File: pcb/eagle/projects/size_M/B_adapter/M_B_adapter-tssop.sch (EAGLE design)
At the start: 16 parts

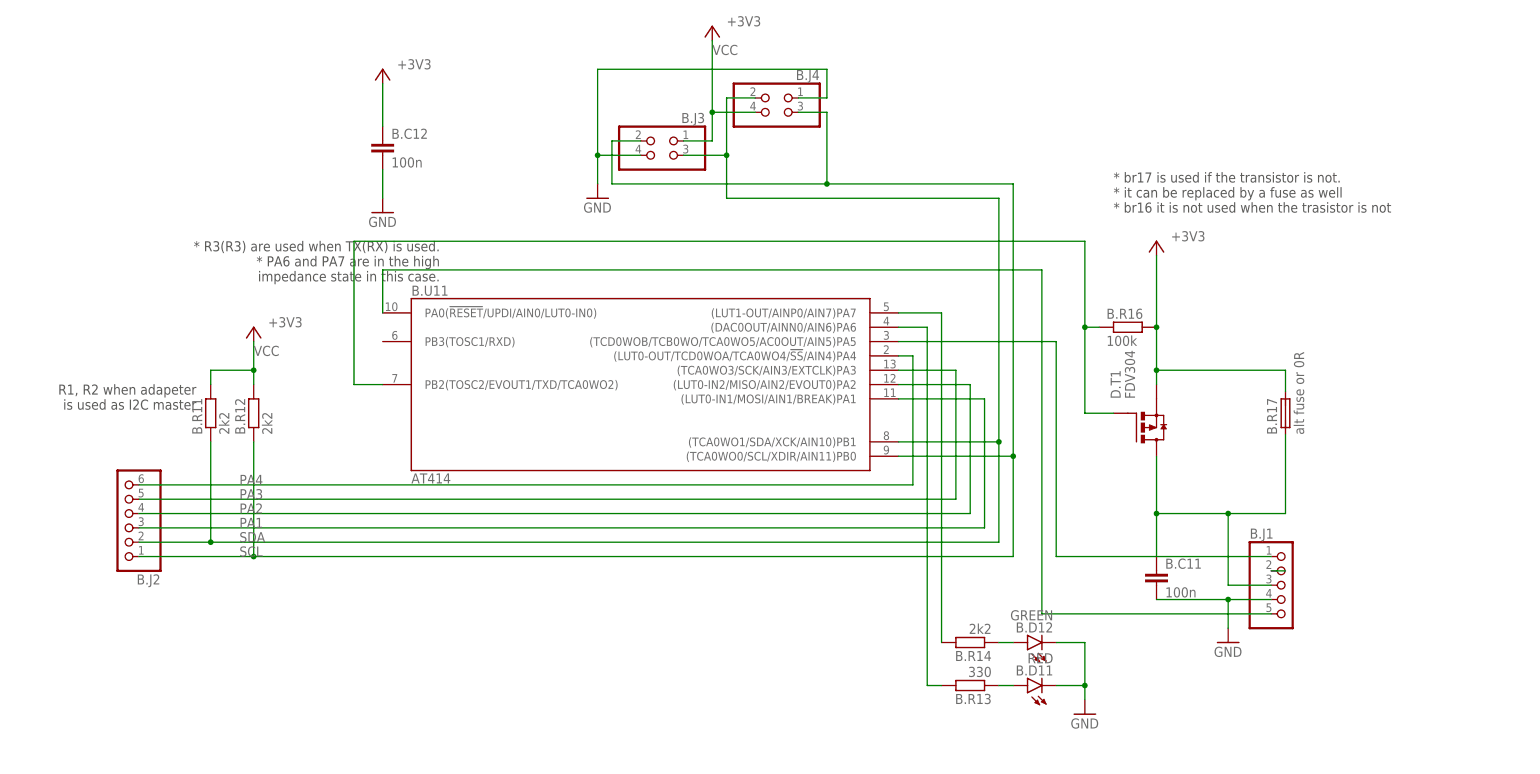
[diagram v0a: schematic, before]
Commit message: changed power sleep transistor to p-channel added tssop version for attiny v2 chips
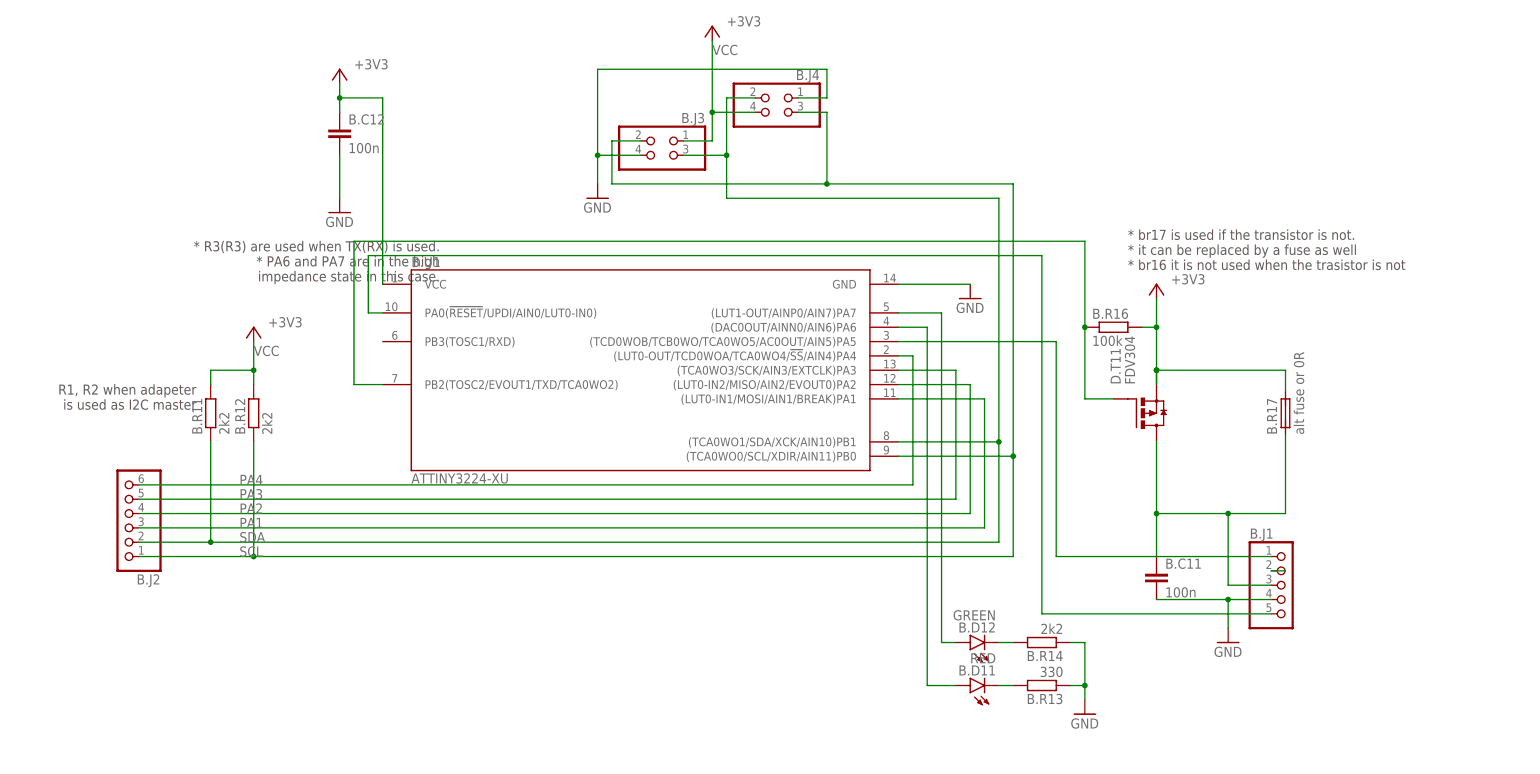
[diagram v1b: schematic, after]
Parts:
- removed B.U11: AT414, atmel:ATTINY414-SSN
- removed D.T1: FDV304, hugo:P-MOSFET
- added B.U1: ATTINY3224-XU, ATTINY412-SSN:ATTINY3224-XU
- added D.T11: FDV304, hugo:P-MOSFET
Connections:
- removed net N$4: B.C11.1, B.J1.3, B.R17.1, D.T1.D
- removed net PA51: B.D11.A, B.R13.1
- new net N$1: B.D12.C, B.R14.2
- new net N$2: B.D11.C, B.R13.2
- net GND: now also B.R13.1, B.R14.1, B.U1.GND; no longer B.D11.C, B.D12.C
- net N$3: now also B.C11.1, B.J1.3, B.R17.1, D.T11.D; no longer B.D12.A, B.R14.1
- net N$5: now also B.D11.A, B.U1.(DAC0OUT/AINN0/AIN6)PA6; no longer B.R13.2, B.U11G$1.(DAC0OUT/AINN0/AIN6)PA6
- net PA1: now also B.U1.(LUT0-IN1/MOSI/AIN1/BREAK)PA1; no longer B.U11G$1.(LUT0-IN1/MOSI/AIN1/BREAK)PA1
- net PA2: now also B.U1.(LUT0-IN2/MISO/AIN2/EVOUT0)PA2; no longer B.U11G$1.(LUT0-IN2/MISO/AIN2/EVOUT0)PA2
- net PA3: now also B.U1.(TCA0WO3/SCK/AIN3/EXTCLK)PA3; no longer B.U11G$1.(TCA0WO3/SCK/AIN3/EXTCLK)PA3
- net PA4: now also B.U1.(LUT0-OUT/TCD0WOA/TCA0WO4/!SS!/AIN4)PA4; no longer B.U11G$1.(LUT0-OUT/TCD0WOA/TCA0WO4/!SS!/AIN4)PA4
- net PA5: now also B.U1.(TCD0WOB/TCB0WO/TCA0WO5/AC0OUT/AIN5)PA5; no longer B.U11G$1.(TCD0WOB/TCB0WO/TCA0WO5/AC0OUT/AIN5)PA5
- net PA7: now also B.D12.A, B.U1.(LUT1-OUT/AINP0/AIN7)PA7; no longer B.R14.2, B.U11G$1.(LUT1-OUT/AINP0/AIN7)PA7
- net PB2: now also B.U1.PB2(TOSC2/EVOUT1/TXD/TCA0WO2), D.T11.G; no longer B.U11G$1.PB2(TOSC2/EVOUT1/TXD/TCA0WO2), D.T1.G
- net SCL: now also B.U1.(TCA0WO0/SCL/XDIR/AIN11)PB0; no longer B.U11G$1.(TCA0WO0/SCL/XDIR/AIN11)PB0
- net SDA: now also B.U1.(TCA0WO1/SDA/XCK/AIN10)PB1; no longer B.U11G$1.(TCA0WO1/SDA/XCK/AIN10)PB1
- net UPDI: now also B.U1.PA0(!RESET!/UPDI/AIN0/LUT0-IN0); no longer B.U11G$1.PA0(!RESET!/UPDI/AIN0/LUT0-IN0)
- net VCC: now also B.U1.VCC, D.T11.S; no longer D.T1.S
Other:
- moved on the sheet: B.C12, B.D11, B.D12, B.R13, B.R14, B.R16

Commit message: version 8 main changes * ideal diode separated 3v3 DC-DC to protect it from back current * smaller package of ina 219 * usage of tssop attiny v2 in adapter * and change of PA5 to PB2 with ^ and ~ (originally used for shield power switch - now PB3) * step motor shield * out signal for BT module
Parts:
- removed B.C11: 100n, rcl:C-EUC0603
- added B.C1: 100n, rcl:C-EUC0603
- renumbered B.C12 to B.C2, B.D11 to B.D1, B.D12 to B.D2, B.R11 to B.R1, B.R12 to B.R2, B.R13 to B.R3, B.R14 to B.R4, B.R16 to B.R6, B.R17 to B.R7, D.T11 to B.T1
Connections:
- removed net PA5: B.J1.1, B.U1.(TCD0WOB/TCB0WO/TCA0WO5/AC0OUT/AIN5)PA5
- new net PB3: B.R6.1, B.T1.G, B.U1.PB3(TOSC1/RXD)
- net GND: now also B.C1.2; no longer B.C11.2
- net N$3: now also B.C1.1; no longer B.C11.1
- net PB2: now also B.J1.1; no longer B.R6.1, B.T1.G

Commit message: PCB v9
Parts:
- removed B.J1: (no value), pinhead2:PINHD-1X5
- added B.J5: (no value), pinhead2:PINHD-1X6
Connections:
- new net PA6: B.J5.1, B.U1.(DAC0OUT/AINN0/AIN6)PA6
- net GND: now also B.J5.4; no longer B.J1.4
- net N$3: now also B.J5.3; no longer B.J1.3
- net N$5: now also B.U1.(TCD0WOB/TCB0WO/TCA0WO5/AC0OUT/AIN5)PA5; no longer B.U1.(DAC0OUT/AINN0/AIN6)PA6
- net PB2: now also B.J5.6; no longer B.J1.1
- net UPDI: now also B.J5.5; no longer B.J1.5
- net VBAT: now also B.J5.2; no longer B.J1.2
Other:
- moved on the sheet: B.D1, B.D2, B.R3, B.R4
